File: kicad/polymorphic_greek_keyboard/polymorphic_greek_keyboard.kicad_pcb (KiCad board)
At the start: 2 copper layers, 1 part, among them U1 ESP32-S2-WROVER

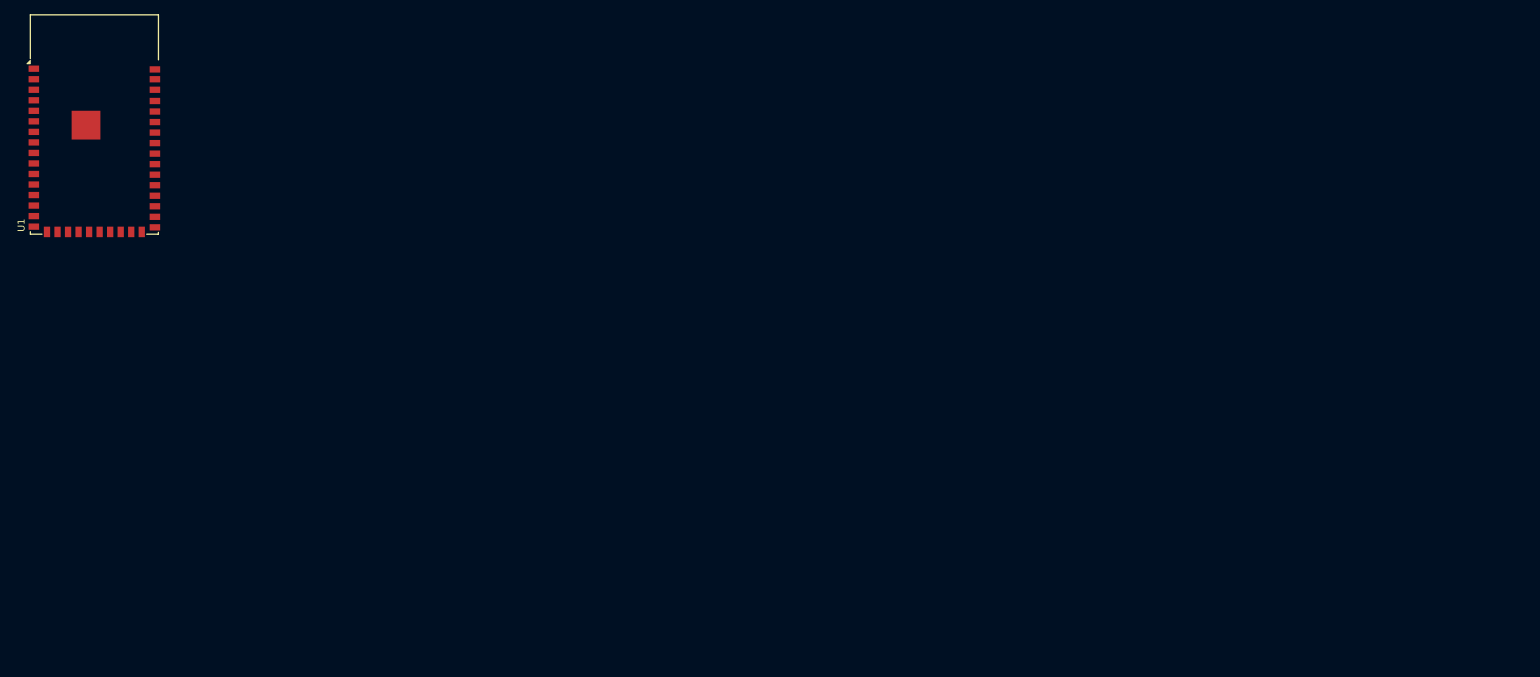
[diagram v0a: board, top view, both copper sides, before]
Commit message: [ADD] child components requied to build the keyboard in subschema's desings in kicad
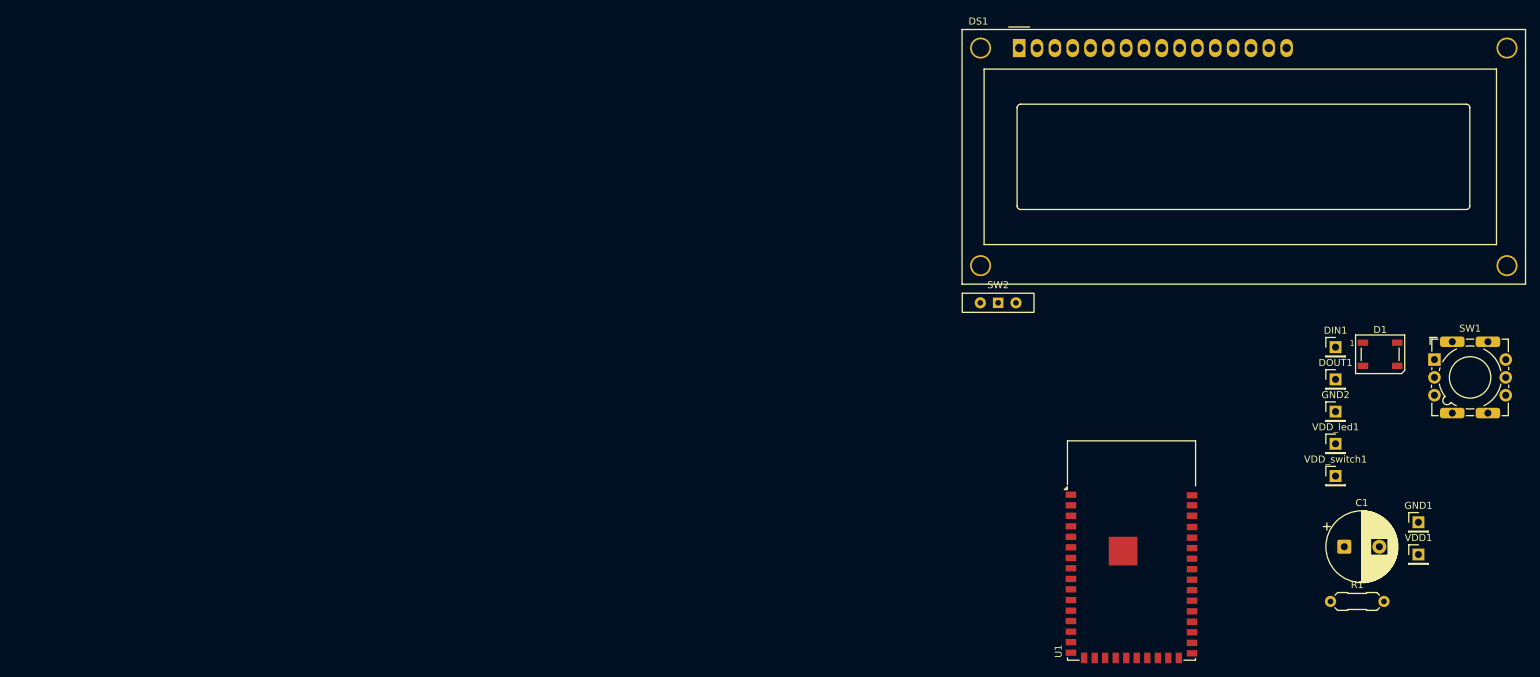
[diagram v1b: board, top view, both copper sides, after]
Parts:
- added C1: 1000uF_16V, Capacitor_THT:CP_Radial_D10.0mm_P5.00mm, F.Cu at (225.4, 112.9)
- added D1: WS2812B, LED_SMD:LED_WS2812B_PLCC4_5.0x5.0mm_P3.2mm, F.Cu at (230.5, 85.5)
- added DIN1: PINHD_1x1_Male, Connector_PinHeader_2.54mm:PinHeader_1x01_P2.54mm_Vertical, F.Cu at (224.2, 84.5)
- added DOUT1: PINHD_1x1_Male, Connector_PinHeader_2.54mm:PinHeader_1x01_P2.54mm_Vertical, F.Cu at (224.2, 89.0)
- added DS1: WC1602A, Display:WC1602A, F.Cu at (179.1, 41.8)
- added GND1: PINHD_1x1_Male, Connector_PinHeader_2.54mm:PinHeader_1x01_P2.54mm_Vertical, F.Cu at (236.0, 109.4)
- added GND2: PINHD_1x1_Male, Connector_PinHeader_2.54mm:PinHeader_1x01_P2.54mm_Vertical, F.Cu at (224.2, 93.6)
- added R1: 330R_0603, PCM_Resistor_THT_AKL:R_Axial_DIN0207_L6.3mm_D2.5mm_P7.62mm_Horizontal, F.Cu at (223.5, 120.7)
- added SW1: SW_SP4T_NR01104, Button_Switch_THT:SW_NKK_NR01, F.Cu at (238.3, 86.2)
- added SW2: SW_Wuerth_450301014042, Button_Switch_THT:SW_Slide-03_Wuerth-WS-SLTV_10x2.5x6.4_P2.54mm, F.Cu at (176.1, 78.1)
- added VDD1: PINHD_1x1_Male, Connector_PinHeader_2.54mm:PinHeader_1x01_P2.54mm_Vertical, F.Cu at (236.0, 114.0)
- added VDD_led1: PINHD_1x1_Male, Connector_PinHeader_2.54mm:PinHeader_1x01_P2.54mm_Vertical, F.Cu at (224.2, 98.2)
- added VDD_switch1: PINHD_1x1_Male, Connector_PinHeader_2.54mm:PinHeader_1x01_P2.54mm_Vertical, F.Cu at (224.2, 102.8)
- moved U1 159.7 mm to (195.1, 117.3)
